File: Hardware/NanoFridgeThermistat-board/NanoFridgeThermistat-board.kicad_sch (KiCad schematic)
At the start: 58 parts, among them J1 Connector_Thermistor, J2 Main_Connector, J3 CompressorMotor_Connector, J4 I2C_Conn, J5 Connector_Thermistor, J6 Connector_Thermistor, SW1 SW_Push, SW2 SW_Push, T1 CST1, U1 MOC3042M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

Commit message: Generated Gerbers files
Signed-off-by: bebenlebricolo <benoittarrade@hotmail.fr>
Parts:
- J5: value Connector_Thermistor -> ConnectorTriacDriver1
- J6: value Connector_Thermistor -> ConnectorTriacDriver2
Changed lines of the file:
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@@
       (effects (font (size 1.27 1.27)) (justify left))
     )
-    (property "Value" "Connector_Thermistor" (at 179.07 26.67 0)
+    (property "Value" "ConnectorTriacDriver2" (at 179.07 26.67 0)
       (effects (font (size 1.27 1.27)) (justify left))
     )
@@
       (effects (font (size 1.27 1.27)) (justify left))
     )
-    (property "Value" "Connector_Thermistor" (at 179.07 20.32 0)
-      (effects (font (size 1.27 1.27)) (justify left))
-    )
+    (property "Value" "ConnectorTriacDriver1" (at 179.07 20.32 0)
+      (effects (font (size 1.27 1.27)) (justify left))
+    )

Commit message: Updated KiCad project files
Signed-off-by: bebenlebricolo <benoittarrade@hotmail.fr>
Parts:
- R14: value 2.2k -> 10k
- R16: value 10k -> 56k
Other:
- note added: "Current transformer used to sense fridge compressor motor current draw. Especially useful to detect stalled motor conditions (when the motor can't start because it can't overcome the resistance from the fluids). The motor pulls a very high current under stalled condition and needs to be detected by the controller. Note : this CT (RS PRO, 75A, 1000:1) shows 0,1V/Amp."
- note removed: "Current transformer used to sense fridge compressor motor current draw. Especially useful to detect stalled motor conditions (when the motor can't start because it can't overcome the resistance from the fluids). The motor pulls a very high current under stalled condition and needs to be detected by the controller"

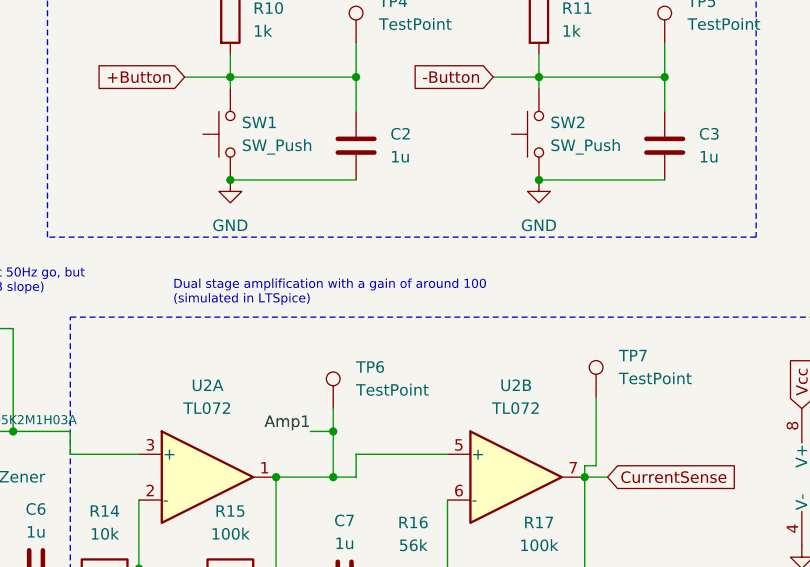
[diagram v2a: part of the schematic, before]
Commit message: Improved current measurements and fixed timing issues ; now RMS is good
Signed-off-by: bebenlebricolo <benoittarrade@hotmail.fr>
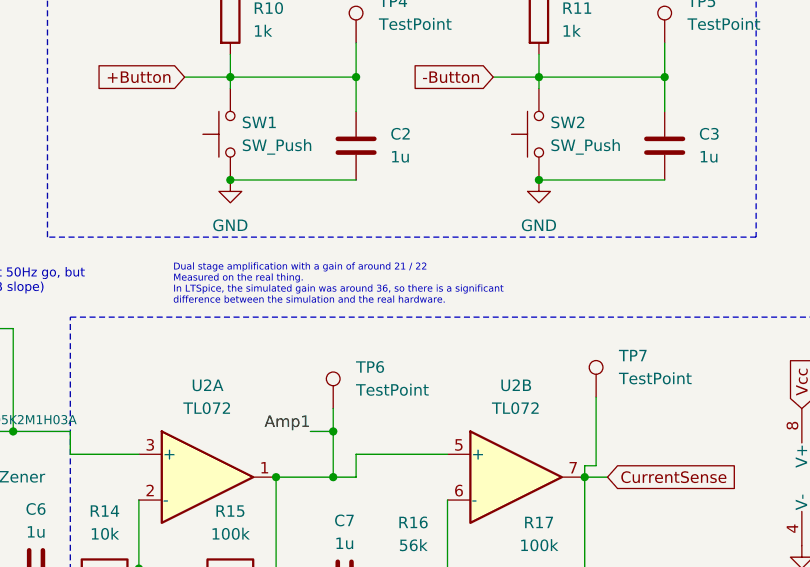
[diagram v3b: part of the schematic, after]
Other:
- note added: "Dual stage amplification with a gain of around 21 / 22 Measured on the real thing. In LTSpice, the simulated gain was around 36, so there is a significant difference between the simulation and the real hardware."
- note removed: "Dual stage amplification with a gain of around 100 (simulated in LTSpice)"
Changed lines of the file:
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@@
 		)
 	)
-	(text "Dual stage amplification with a gain of around 100 \n(simulated in LTSpice)"
+	(text "Dual stage amplification with a gain of around 21 / 22 \nMeasured on the real thing.\nIn LTSpice, the simulated gain was around 36, so there is a significant\ndifference between the simulation and the real hardware."
 		(exclude_from_sim no)
 		(at 143.51 127 0)
 		(effects
 			(font
-				(size 1 1)
+				(size 0.762 0.762)
 			)
 			(justify left bottom)
